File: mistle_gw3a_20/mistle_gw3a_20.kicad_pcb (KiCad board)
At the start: 2 copper layers, 110 x 67 mm, 174 parts, among them J1 SWD, J11 Joystick 0, J12 Joystick 1, J13 USB_A_Stacked, J2 USB_C_Receptacle_USB2.0, J3 JTAG, J4 Micro_SD_Card_Det1, J5 HDMI_A, J6 Grove 1125S-4P, J7 USB_A_Stacked, J8 EXT UART, SW1 Boot, SW2 KEY1, SW3 KEY2, U1 SY8113BADC, U10 74LCX07, U11 RP2350_60QFN, U13 MT48LC16M16A2TG, U2 W25Q64JVS, U3 USBLC6-2SC6, U5 CH334P, U6 W25Q64JVS, U7 GW3A-LV20-Q144, U8 SY8113BADC, U9 74LCX07, Y1 12MHz, Y2 50MHz, Y3 12MHz

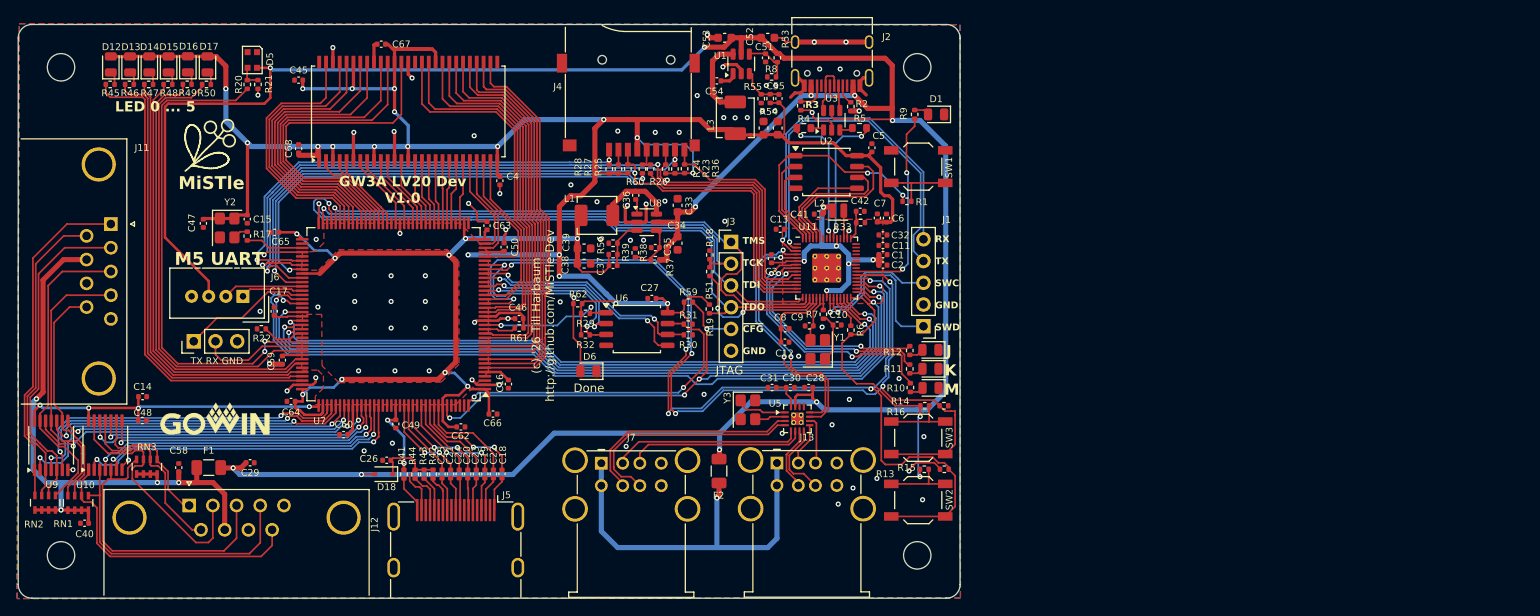
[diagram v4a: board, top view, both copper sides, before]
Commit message: Add expansion connector
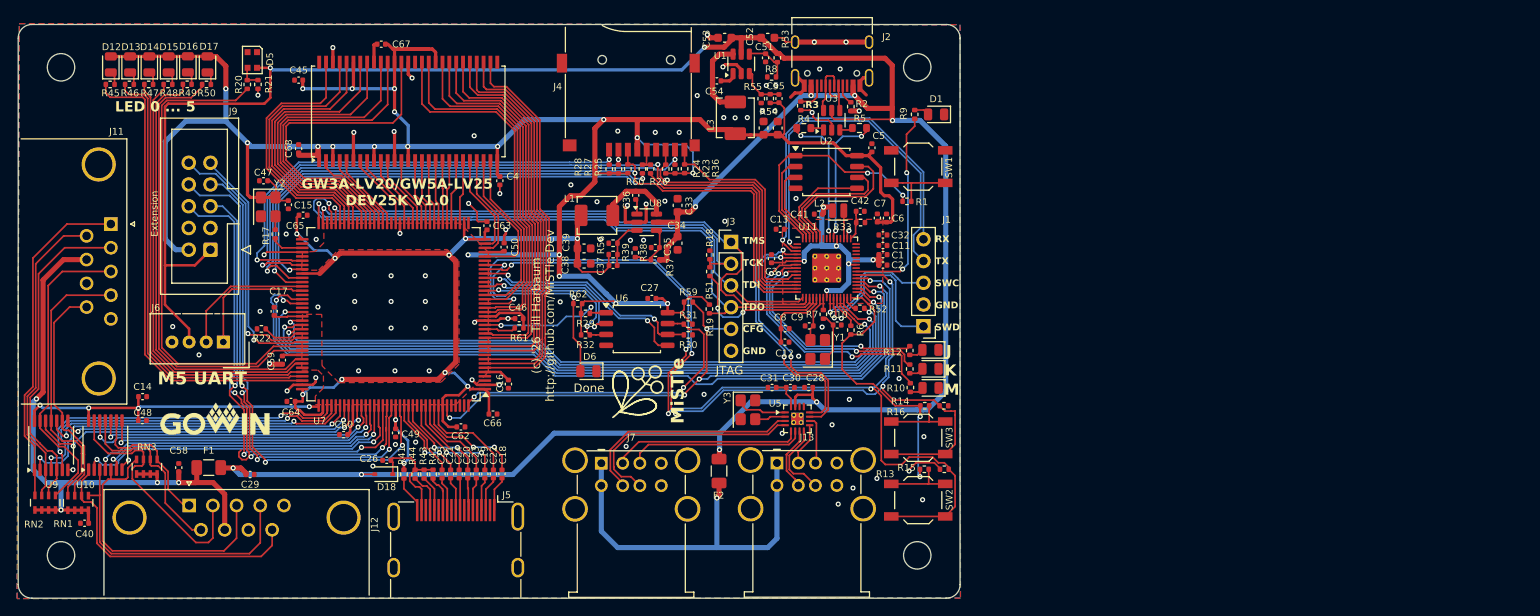
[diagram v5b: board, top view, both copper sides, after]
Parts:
- removed J8: EXT UART, Connector_PinHeader_2.54mm:PinHeader_1x03_P2.54mm_Vertical
- added J9: EXT, Connector_IDC:IDC-Header_2x05_P2.54mm_Vertical, F.Cu at (102.5, 66.3)
- added R52: 22, Resistor_SMD:R_0402_1005Metric, F.Cu at (178.3, 73.2)
- moved C47 8.61 mm to (108.7, 58.2), turned to 0 degrees
- moved J6 5.80 mm to (104.0, 77.1)
- moved Y2 5.40 mm to (109.2, 61.3)
- moved C15 5.09 mm to (111.5, 61.0)
- moved C65 3.88 mm to (113.3, 62.3), turned to 0 degrees
- moved R17 3.28 mm to (110.0, 64.5)
- moved C29 1.37 mm to (107.1, 92.6)
- moved C49 1.05 mm to (124.1, 87.7)
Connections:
- U11 pad 29: SCK -> Net-(U11-GPIO18)
- U7 pad 124: unconnected-(U7I-IOL16A-Pad124) -> EXT0
- U7 pad 125: unconnected-(U7I-IOL16B-Pad125) -> EXT1
- U7 pad 126: unconnected-(U7I-IOL18A-Pad126) -> EXT2
- U7 pad 128: unconnected-(U7I-IOL18B-Pad128) -> EXT3
- U7 pad 86: MON_TX -> unconnected-(U7C-IOT52B-Pad86)
- U7 pad 96: unconnected-(U7J-IOT27B-Pad96) -> EXT5
- U7 pad 97: WS2812 -> EXT4
- U7 pad 98: MON_RX -> WS2812
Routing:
- net EXT3: track 0.00 -> 59.9 mm, vias 0 -> 3
- net EXT1: track 0.00 -> 58.5 mm, vias 0 -> 3
- net EXT2: track 0.00 -> 57.0 mm, vias 0 -> 3
- net EXT0: track 0.00 -> 54.0 mm, vias 0 -> 3
- net EXT5: track 0.00 -> 30.8 mm, vias 0 -> 1
- net EXT4: track 0.00 -> 28.7 mm, vias 0 -> 1
- net +3.3V: track 382.5 -> 406.2 mm
- net MON_TX: track 15.2 -> 0.00 mm
- net MON_RX: track 12.6 -> 0.00 mm
- net +5V: track 317.3 -> 327.9 mm
- net MIDI_IN: track 7.34 -> 14.9 mm
- net MIDI_OUT: track 9.40 -> 16.0 mm
- net /GW3A-LV20 FPGA/Interfaces/CLK50: track 6.78 -> 3.80 mm
- net SCK: track 83.3 -> 80.6 mm
- net Net-(U11-GPIO18): track 0.00 -> 1.83 mm
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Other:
- board text added: "Extension"
- board text added: "GW3A-LV20/GW5A-LV25 DEV25K V1.0"
- board text removed: "GW3A LV20 Dev V1.0"
- board text removed: "TX RX GND"
